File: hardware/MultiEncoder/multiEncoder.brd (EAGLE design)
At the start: 100 x 80 mm, 21 parts, among them J1 90325-0004, J2 90325-0004, J3 90325-0004, J4 90325-0004, U1 MCP23017-E/SP

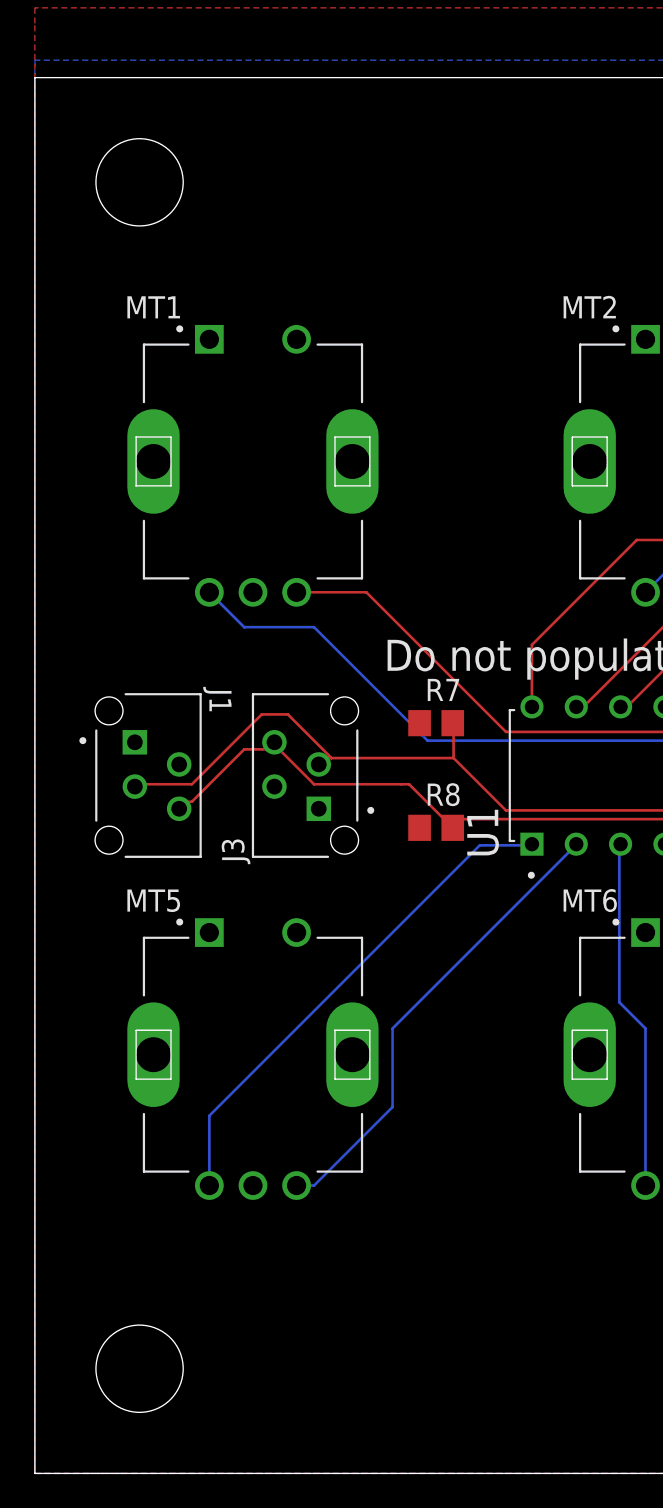
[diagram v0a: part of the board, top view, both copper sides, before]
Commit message: add vertical connection option
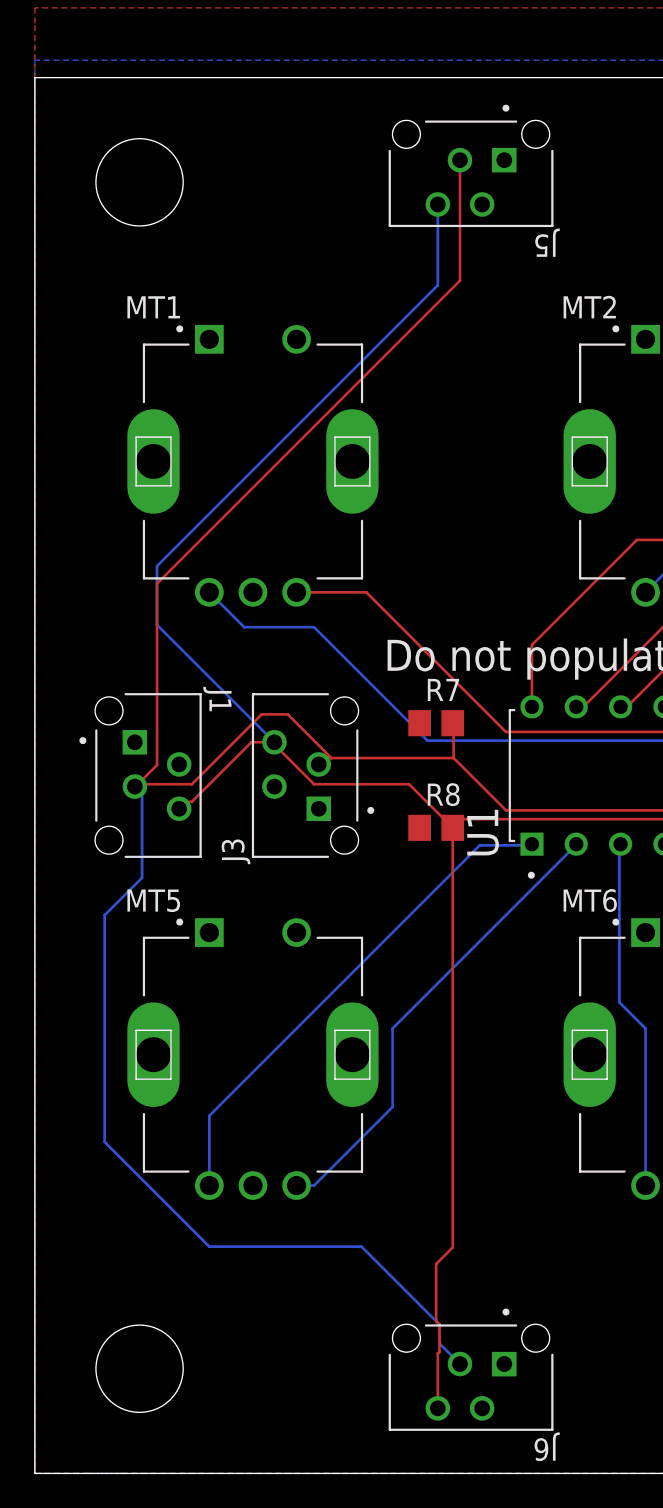
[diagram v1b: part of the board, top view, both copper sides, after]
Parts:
- added J5, J6: 90325-0004, 90325-0004:MOLEX_90325-0004
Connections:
- net GND: now also J5.2, J6.2
- net SCL: now also J5.3, J6.3
- net SDA: now also J5.4, J6.4
- net VCC: now also J5.1, J6.1
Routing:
- net SCL: track 110.7 -> 202.0 mm
- net SDA: track 97.9 -> 171.9 mm
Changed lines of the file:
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@@
 <attribute name="VALUE" x="53.94563125" y="41.1171" size="1.78091875" layer="27" rot="R180"/>
+</element>
+<element name="J5" library="90325-0004" package="MOLEX_90325-0004" value="90325-0004" x="25" y="74" smashed="yes" rot="R180">
+<attribute name="AVAILABILITY" value="In Stock" x="37" y="62" size="1.778" layer="27" rot="R180" display="off"/>
+<attribute name="DESCRIPTION" value=" HEADER, PICOFLEX, 4WAY; Connector Type:Wire-to-Board; Gender:Pin; Ways, No. of:4; Lead Spacing:1.27mm; Termination Method:Solder; Contact Material:Brass; Series:PICOFLEX PF50; Contact Plating:Tin; Rows, No. of:1; Colour:Black; Current Rating:1.2A; Flammability Rating:UL94V-0; Material:Polyester; No. of Poles:4; Pitch:1.27mm; Resistance, Contact:10mohm; Temp, Op. Max:105°C; Temp, Op. Min:-25°C; Voltage Rating, AC:250V; Voltage, Withstand:750V; Voltage, Working:250V; Width, External:3.81mm; Wire Size, AWG Max:26AWG; Wire Size, AWG Min:28AWG; Fixing Centres:7.41mm " x="37" y="62" size="1.778" layer="27" rot="R180" display="off"/>
+<attribute name="MF" value="Molex" x="37" y="62" size="1.778" layer="27" rot="R180" display="off"/>
+<attribute name="MP" value="90325-0004" x="37" y="62" size="1.778" layer="27" rot="R180" display="off"/>
+<attribute name="NAME" x="30" y="71" size="1.27" layer="25" ratio="10" rot="SR180"/>
+<attribute name="PACKAGE" value="None" x="37" y="62" size="1.778" layer="27" rot="R180" display="off"/>
+<attribute name="PRICE" value="None" x="37" y="62" size="1.778" layer="27" rot="R180" display="off"/>
+<attribute name="PURCHASE-URL" value="https://pricing.snapeda.com/search/part/90325-0004/?ref=eda" x="37" y="62" size="1.778" layer="27" rot="R180" display="off"/>
+<attribute name="VALUE" x="30" y="78.5" size="1.27" layer="27" ratio="10" rot="SR180" align="top-left"/>
+</element>
+<element name="J6" library="90325-0004" package="MOLEX_90325-0004" value="90325-0004" x="25" y="5" smashed="yes" rot="R180">
+<attribute name="AVAILABILITY" value="In Stock" x="48" y="-19" size="1.778" layer="27" rot="R180" display="off"/>
+<attribute name="DESCRIPTION" value=" HEADER, PICOFLEX, 4WAY; Connector Type:Wire-to-Board; Gender:Pin; Ways, No. of:4; Lead Spacing:1.27mm; Termination Method:Solder; Contact Material:Brass; Series:PICOFLEX PF50; Contact Plating:Tin; Rows, No. of:1; Colour:Black; Current Rating:1.2A; Flammability Rating:UL94V-0; Material:Polyester; No. of Poles:4; Pitch:1.27mm; Resistance, Contact:10mohm; Temp, Op. Max:105°C; Temp, Op. Min:-25°C; Voltage Rating, AC:250V; Voltage, Withstand:750V; Voltage, Working:250V; Width, External:3.81mm; Wire Size, AWG Max:26AWG; Wire Size, AWG Min:28AWG; Fixing Centres:7.41mm " x="48" y="-19" size="1.778" layer="27" rot="R180" display="off"/>
+<attribute name="MF" value="Molex" x="48" y="-19" size="1.778" layer="27" rot="R180" display="off"/>
+<attribute name="MP" value="90325-0004" x="48" y="-19" size="1.778" layer="27" rot="R180" display="off"/>
+<attribute name="NAME" x="30" y="2" size="1.27" layer="25" ratio="10" rot="SR180"/>
+<attribute name="PACKAGE" value="None" x="48" y="-19" size="1.778" layer="27" rot="R180" display="off"/>
+<attribute name="PRICE" value="None" x="48" y="-19" size="1.778" layer="27" rot="R180" display="off"/>
+<attribute name="PURCHASE-URL" value="https://pricing.snapeda.com/search/part/90325-0004/?ref=eda" x="48" y="-19" size="1.778" layer="27" rot="R180" display="off"/>
+<attribute name="VALUE" x="30" y="9.5" size="1.27" layer="27" ratio="10" rot="SR180" align="top-left"/>
 </element>
 </elements>
@@
 <wire x1="75" y1="36.5" x2="75" y2="36.05" width="0.1524" layer="1"/>
 <wire x1="80.5" y1="39" x2="80.73" y2="39.365" width="0.1524" layer="1"/>
+<contactref element="J5" pad="2"/>
+<contactref element="J6" pad="2"/>
 </signal>
 <signal name="VCC">
@@
 <contactref element="U1" pad="18"/>
 <contactref element="U1" pad="9"/>
+<contactref element="J5" pad="1"/>
+<contactref element="J6" pad="1"/>
 </signal>
 <signal name="SCL">
@@
 <wire x1="14.5" y1="43.5" x2="13" y2="43.5" width="0.1524" layer="1"/>
 <wire x1="17" y1="41" x2="14.5" y2="43.5" width="0.1524" layer="1"/>
-<wire x1="6" y1="39.5" x2="5.73" y2="39.365" width="0.1524" layer="1"/>
+<wire x1="6" y1="39.5" x2="5.8" y2="39.4" width="0.1524" layer="1"/>
+<wire x1="5.8" y1="39.4" x2="5.73" y2="39.365" width="0.1524" layer="1"/>
 <wire x1="59" y1="33.5" x2="56.5" y2="36" width="0.1524" layer="1"/>
 <wire x1="76.5" y1="33.5" x2="66" y2="33.5" width="0.1524" layer="1"/>
@@
 <wire x1="61.5" y1="38" x2="27" y2="38" width="0.1524" layer="1"/>
 <wire x1="66" y1="33.5" x2="61.5" y2="38" width="0.1524" layer="1"/>
+<contactref element="J5" pad="3"/>
+<contactref element="J6" pad="3"/>
+<wire x1="24.365" y1="75.27" x2="24.365" y2="68.365" width="0.1524" layer="1"/>
+<wire x1="7" y1="40.6" x2="5.8" y2="39.4" width="0.1524" layer="1"/>
+<wire x1="24.365" y1="68.365" x2="7" y2="51" width="0.1524" layer="1"/>
+<wire x1="7" y1="51" x2="7" y2="40.6" width="0.1524" layer="1"/>
+<wire x1="24.365" y1="6.27" x2="23.1872" y2="7.4478" width="0.1524" layer="16"/>
+<wire x1="23.1872" y1="7.4478" x2="23.1872" y2="8.533775" width="0.1524" layer="16"/>
+<wire x1="23.1872" y1="8.533775" x2="18.720975" y2="13" width="0.1524" layer="16"/>
+<wire x1="18.720975" y1="13" x2="10" y2="13" width="0.1524" layer="16"/>
+<wire x1="10" y1="13" x2="4" y2="19" width="0.1524" layer="16"/>
+<wire x1="6.1422" y1="34.1422" x2="6.1422" y2="38.9528" width="0.1524" layer="16"/>
+<wire x1="6.1422" y1="38.9528" x2="5.73" y2="39.365" width="0.1524" layer="16"/>
+<wire x1="4" y1="19" x2="4" y2="32" width="0.1524" layer="16"/>
+<wire x1="4" y1="32" x2="6.1422" y2="34.1422" width="0.1524" layer="16"/>
 </signal>
 <signal name="SDA">
@@
 <contactref element="U1" pad="13"/>
 <wire x1="24" y1="37.5" x2="24" y2="37" width="0.1524" layer="1"/>
-<wire x1="16" y1="39.5" x2="21" y2="39.5" width="0.1524" layer="1"/>
+<wire x1="16" y1="39.5" x2="21.45" y2="39.5" width="0.1524" layer="1"/>
 <wire x1="14" y1="41.5" x2="16" y2="39.5" width="0.1524" layer="1"/>
 <wire x1="24" y1="37" x2="23.95" y2="37" width="0.1524" layer="1"/>
 <wire x1="14" y1="41.5" x2="13.73" y2="41.905" width="0.1524" layer="1"/>
-<wire x1="9" y1="38.5" x2="8.5" y2="38.5" width="0.1524" layer="1"/>
-<wire x1="12" y1="41.5" x2="9" y2="38.5" width="0.1524" layer="1"/>
-<wire x1="13.5" y1="41.5" x2="12" y2="41.5" width="0.1524" layer="1"/>
+<wire x1="8.5" y1="38.5" x2="9" y2="38.5" width="0.1524" layer="1"/>
 <wire x1="8.5" y1="38.5" x2="8.27" y2="38.095" width="0.1524" layer="1"/>
-<wire x1="13.5" y1="41.5" x2="13.73" y2="41.905" width="0.1524" layer="1"/>
 <wire x1="60.5" y1="34.5" x2="59" y2="36" width="0.1524" layer="16"/>
 <wire x1="73" y1="34.5" x2="60.5" y2="34.5" width="0.1524" layer="16"/>
@@
 <wire x1="58.5" y1="36.5" x2="58.97" y2="36.065" width="0.1524" layer="1"/>
 <wire x1="23.95" y1="37" x2="21.45" y2="39.5" width="0.1524" layer="1"/>
-<wire x1="21.45" y1="39.5" x2="21" y2="39.5" width="0.1524" layer="1"/>
+<contactref element="J5" pad="4"/>
+<contactref element="J6" pad="4"/>
+<wire x1="23.95" y1="37" x2="23.95" y2="12.95" width="0.1524" layer="1"/>
+<wire x1="23.95" y1="12.95" x2="23" y2="12" width="0.1524" layer="1"/>
+<wire x1="23" y1="12" x2="23" y2="8.720975" width="0.1524" layer="1"/>
+<wire x1="23" y1="8.720975" x2="23.1872" y2="8.533775" width="0.1524" layer="1"/>
+<wire x1="23.1872" y1="8.533775" x2="23.1872" y2="6.966225" width="0.1524" layer="1"/>
+<wire x1="23.1872" y1="6.966225" x2="23.095" y2="6.874025" width="0.1524" layer="1"/>
+<wire x1="23.095" y1="6.874025" x2="23.095" y2="3.73" width="0.1524" layer="1"/>
+<wire x1="12.405" y1="41.905" x2="13.73" y2="41.905" width="0.1524" layer="1"/>
+<wire x1="9" y1="38.5" x2="12.405" y2="41.905" width="0.1524" layer="1"/>
+<wire x1="23.095" y1="72.73" x2="23.095" y2="68.095" width="0.1524" layer="16"/>
+<wire x1="23.095" y1="68.095" x2="7" y2="52" width="0.1524" layer="16"/>
+<wire x1="7" y1="52" x2="7" y2="48.635" width="0.1524" layer="16"/>
+<wire x1="7" y1="48.635" x2="13.73" y2="41.905" width="0.1524" layer="16"/>
 </signal>
 <signal name="A2">
